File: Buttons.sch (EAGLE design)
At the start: 63 parts, among them T1 SI2301, U1 TCA8418RTWR, U2 Tiny85-20-SMT

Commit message: this could be the one neo!
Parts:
- added R3: 1k, SparkFun-Passives:RESISTOR0805-RES
- R1: value 100 -> 1k
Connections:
- removed net N$49: U1.ROW0
- removed net N$9: U1.ROW1
- new net N$8: R3.2, U1.ROW5, U1.ROW6, U1.ROW7
- net 3V3@2: now also R3.1
- net N$24: now also U1.ROW4; no longer U1.ROW6
- net N$29: now also U1.ROW3; no longer U1.ROW5
- net N$30: now also U1.ROW2; no longer U1.ROW4
- net N$31: now also U1.ROW1; no longer U1.ROW3
- net N$33: now also U1.ROW0; no longer U1.ROW2
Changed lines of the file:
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@@
 <parts>
 <part name="U$2" library="ili9341" deviceset="ILI9341-2.8" device=""/>
-<part name="R1" library="resistor" deviceset="R-EU_" device="R0805" value="100"/>
+<part name="R1" library="resistor" deviceset="R-EU_" device="R0805" value="1k"/>
 <part name="GND3" library="supply1" deviceset="GND" device=""/>
 <part name="PI1" library="RPI-Zero" deviceset="RPI-ZERO" device=""/>
@@
 <part name="U$3" library="5mmSNAP" deviceset="5MMSNAP" device=""/>
 <part name="GND10" library="supply1" deviceset="GND" device=""/>
+<part name="R3" library="SparkFun-Passives" deviceset="RESISTOR" device="0805-RES" value="1k"/>
 </parts>
 <sheets>
@@
 <instance part="GND4" gate="1" x="48.26" y="200.66"/>
 <instance part="GND5" gate="1" x="63.5" y="187.96"/>
-<instance part="GND6" gate="1" x="-53.34" y="78.74" rot="R270"/>
+<instance part="GND6" gate="1" x="-38.1" y="78.74" rot="R270"/>
 <instance part="GND9" gate="1" x="180.34" y="182.88" rot="R90"/>
 <instance part="U1" gate="A" x="-15.24" y="99.06"/>
@@
 <instance part="U$3" gate="G$1" x="93.98" y="210.82" rot="R180"/>
 <instance part="GND10" gate="1" x="182.88" y="233.68" rot="R180"/>
+<instance part="R3" gate="G$1" x="-45.72" y="73.66" rot="R90"/>
 </instances>
 <busses>
@@
 <pinref part="U1" gate="A" pin="GND"/>
 <pinref part="GND6" gate="1" pin="GND"/>
-<wire x1="-50.8" y1="78.74" x2="-33.02" y2="78.74" width="0.1524" layer="91"/>
+<wire x1="-35.56" y1="78.74" x2="-33.02" y2="78.74" width="0.1524" layer="91"/>
 </segment>
 <segment>
@@
 <net name="N$24" class="0">
 <segment>
-<pinref part="U1" gate="A" pin="ROW6"/>
-<wire x1="-33.02" y1="86.36" x2="-35.56" y2="86.36" width="0.1524" layer="91"/>
-<wire x1="-35.56" y1="86.36" x2="-35.56" y2="66.04" width="0.1524" layer="91"/>
-<wire x1="-35.56" y1="66.04" x2="5.08" y2="66.04" width="0.1524" layer="91"/>
+<wire x1="-50.8" y1="91.44" x2="-50.8" y2="66.04" width="0.1524" layer="91"/>
+<wire x1="-50.8" y1="66.04" x2="5.08" y2="66.04" width="0.1524" layer="91"/>
 <wire x1="5.08" y1="66.04" x2="5.08" y2="71.12" width="0.1524" layer="91"/>
 <wire x1="5.08" y1="71.12" x2="33.02" y2="71.12" width="0.1524" layer="91"/>
@@
 <pinref part="A9" gate="G$1" pin="P$2"/>
 <wire x1="147.32" y1="73.66" x2="147.32" y2="71.12" width="0.1524" layer="91"/>
+<pinref part="U1" gate="A" pin="ROW4"/>
+<wire x1="-33.02" y1="91.44" x2="-50.8" y2="91.44" width="0.1524" layer="91"/>
 </segment>
 </net>
 <net name="N$29" class="0">
 <segment>
-<pinref part="U1" gate="A" pin="ROW5"/>
-<wire x1="-38.1" y1="55.88" x2="-38.1" y2="88.9" width="0.1524" layer="91"/>
-<wire x1="-38.1" y1="88.9" x2="-33.02" y2="88.9" width="0.1524" layer="91"/>
+<wire x1="-53.34" y1="55.88" x2="-53.34" y2="93.98" width="0.1524" layer="91"/>
 <wire x1="147.32" y1="55.88" x2="134.62" y2="55.88" width="0.1524" layer="91"/>
 <pinref part="B9" gate="G$1" pin="P$2"/>
@@
 <wire x1="58.42" y1="55.88" x2="45.72" y2="55.88" width="0.1524" layer="91"/>
 <wire x1="45.72" y1="55.88" x2="33.02" y2="55.88" width="0.1524" layer="91"/>
-<wire x1="33.02" y1="55.88" x2="-38.1" y2="55.88" width="0.1524" layer="91"/>
+<wire x1="33.02" y1="55.88" x2="-53.34" y2="55.88" width="0.1524" layer="91"/>
 <wire x1="147.32" y1="58.42" x2="147.32" y2="55.88" width="0.1524" layer="91"/>
 <pinref part="B8" gate="G$1" pin="P$2"/>
@@
 <pinref part="B0" gate="G$1" pin="P$2"/>
 <wire x1="33.02" y1="58.42" x2="33.02" y2="55.88" width="0.1524" layer="91"/>
+<pinref part="U1" gate="A" pin="ROW3"/>
+<wire x1="-33.02" y1="93.98" x2="-53.34" y2="93.98" width="0.1524" layer="91"/>
 </segment>
 </net>
 <net name="N$30" class="0">
 <segment>
-<pinref part="U1" gate="A" pin="ROW4"/>
-<wire x1="-40.64" y1="40.64" x2="-40.64" y2="91.44" width="0.1524" layer="91"/>
-<wire x1="-40.64" y1="91.44" x2="-33.02" y2="91.44" width="0.1524" layer="91"/>
+<wire x1="-55.88" y1="40.64" x2="-55.88" y2="96.52" width="0.1524" layer="91"/>
 <wire x1="147.32" y1="40.64" x2="134.62" y2="40.64" width="0.1524" layer="91"/>
 <pinref part="C0" gate="G$1" pin="P$2"/>
@@
 <wire x1="58.42" y1="40.64" x2="45.72" y2="40.64" width="0.1524" layer="91"/>
 <wire x1="45.72" y1="40.64" x2="33.02" y2="40.64" width="0.1524" layer="91"/>
-<wire x1="33.02" y1="40.64" x2="-40.64" y2="40.64" width="0.1524" layer="91"/>
+<wire x1="33.02" y1="40.64" x2="-55.88" y2="40.64" width="0.1524" layer="91"/>
 <wire x1="33.02" y1="43.18" x2="33.02" y2="40.64" width="0.1524" layer="91"/>
 <pinref part="C1" gate="G$1" pin="P$2"/>
@@
 <pinref part="C9" gate="G$1" pin="P$2"/>
 <wire x1="147.32" y1="43.18" x2="147.32" y2="40.64" width="0.1524" layer="91"/>
+<pinref part="U1" gate="A" pin="ROW2"/>
+<wire x1="-33.02" y1="96.52" x2="-55.88" y2="96.52" width="0.1524" layer="91"/>
 </segment>
 </net>
 <net name="N$31" class="0">
 <segment>
-<pinref part="U1" gate="A" pin="ROW3"/>
-<wire x1="-33.02" y1="93.98" x2="-43.18" y2="93.98" width="0.1524" layer="91"/>
-<wire x1="-43.18" y1="93.98" x2="-43.18" y2="25.4" width="0.1524" layer="91"/>
+<wire x1="-58.42" y1="99.06" x2="-58.42" y2="25.4" width="0.1524" layer="91"/>
 <wire x1="147.32" y1="25.4" x2="134.62" y2="25.4" width="0.1524" layer="91"/>
 <pinref part="D9" gate="G$1" pin="P$2"/>
@@
 <wire x1="58.42" y1="25.4" x2="45.72" y2="25.4" width="0.1524" layer="91"/>
 <wire x1="45.72" y1="25.4" x2="33.02" y2="25.4" width="0.1524" layer="91"/>
-<wire x1="33.02" y1="25.4" x2="-43.18" y2="25.4" width="0.1524" layer="91"/>
+<wire x1="33.02" y1="25.4" x2="-58.42" y2="25.4" width="0.1524" layer="91"/>
 <wire x1="147.32" y1="27.94" x2="147.32" y2="25.4" width="0.1524" layer="91"/>
 <pinref part="D8" gate="G$1" pin="P$2"/>
@@
 <pinref part="D0" gate="G$1" pin="P$2"/>
 <wire x1="33.02" y1="27.94" x2="33.02" y2="25.4" width="0.1524" layer="91"/>
+<pinref part="U1" gate="A" pin="ROW1"/>
+<wire x1="-33.02" y1="99.06" x2="-58.42" y2="99.06" width="0.1524" layer="91"/>
 </segment>
 </net>
 <net name="N$33" class="0">
 <segment>
-<pinref part="U1" gate="A" pin="ROW2"/>
-<wire x1="-45.72" y1="10.16" x2="-45.72" y2="96.52" width="0.1524" layer="91"/>
-<wire x1="-45.72" y1="96.52" x2="-33.02" y2="96.52" width="0.1524" layer="91"/>
+<wire x1="-60.96" y1="10.16" x2="-60.96" y2="101.6" width="0.1524" layer="91"/>
 <wire x1="147.32" y1="10.16" x2="134.62" y2="10.16" width="0.1524" layer="91"/>
 <pinref part="E0" gate="G$1" pin="P$2"/>
@@
 <wire x1="58.42" y1="10.16" x2="45.72" y2="10.16" width="0.1524" layer="91"/>
 <wire x1="45.72" y1="10.16" x2="33.02" y2="10.16" width="0.1524" layer="91"/>
-<wire x1="33.02" y1="10.16" x2="-45.72" y2="10.16" width="0.1524" layer="91"/>
+<wire x1="33.02" y1="10.16" x2="-60.96" y2="10.16" width="0.1524" layer="91"/>
 <wire x1="33.02" y1="12.7" x2="33.02" y2="10.16" width="0.1524" layer="91"/>
 <pinref part="E1" gate="G$1" pin="P$2"/>
@@
 <pinref part="E9" gate="G$1" pin="P$2"/>
 <wire x1="147.32" y1="12.7" x2="147.32" y2="10.16" width="0.1524" layer="91"/>
+<pinref part="U1" gate="A" pin="ROW0"/>
+<wire x1="-33.02" y1="101.6" x2="-60.96" y2="101.6" width="0.1524" layer="91"/>
 </segment>
 </net>
@@
 </segment>
 </net>
-<net name="N$9" class="0">
-<segment>
-<pinref part="U1" gate="A" pin="ROW1"/>
-<wire x1="-48.26" y1="99.06" x2="-33.02" y2="99.06" width="0.1524" layer="91"/>
-</segment>
-</net>
-<net name="N$49" class="0">
-<segment>
-<pinref part="U1" gate="A" pin="ROW0"/>
-<wire x1="-50.8" y1="101.6" x2="-33.02" y2="101.6" width="0.1524" layer="91"/>
-</segment>
-</net>
 <net name="N$10" class="0">
 <segment>
@@
 <pinref part="U1" gate="A" pin="VCC"/>
 <pinref part="PI1" gate="G$1" pin="3V3@2"/>
-<wire x1="-33.02" y1="177.8" x2="-33.02" y2="114.3" width="0.1524" layer="91"/>
+<wire x1="-33.02" y1="177.8" x2="-33.02" y2="124.46" width="0.1524" layer="91"/>
+<wire x1="-33.02" y1="124.46" x2="-33.02" y2="114.3" width="0.1524" layer="91"/>
 <wire x1="106.68" y1="177.8" x2="-33.02" y2="177.8" width="0.1524" layer="91"/>
-</segment>
-</net>
+<wire x1="-45.72" y1="68.58" x2="-15.24" y2="68.58" width="0.1524" layer="91"/>
+<wire x1="-15.24" y1="68.58" x2="-15.24" y2="124.46" width="0.1524" layer="91"/>
+<wire x1="-15.24" y1="124.46" x2="-33.02" y2="124.46" width="0.1524" layer="91"/>
+<pinref part="R3" gate="G$1" pin="1"/>
+</segment>
+</net>
+<net name="N$8" class="0">
+<segment>
+<pinref part="U1" gate="A" pin="ROW5"/>
+<wire x1="-33.02" y1="88.9" x2="-45.72" y2="88.9" width="0.1524" layer="91"/>
+<wire x1="-45.72" y1="88.9" x2="-45.72" y2="86.36" width="0.1524" layer="91"/>
+<pinref part="U1" gate="A" pin="ROW7"/>
+<pinref part="U1" gate="A" pin="ROW6"/>
+<wire x1="-33.02" y1="86.36" x2="-45.72" y2="86.36" width="0.1524" layer="91"/>
+<wire x1="-45.72" y1="78.74" x2="-45.72" y2="83.82" width="0.1524" layer="91"/>
+<wire x1="-45.72" y1="83.82" x2="-45.72" y2="86.36" width="0.1524" layer="91"/>
+<wire x1="-33.02" y1="83.82" x2="-45.72" y2="83.82" width="0.1524" layer="91"/>
+<pinref part="R3" gate="G$1" pin="2"/>
+</segment>
+</net>

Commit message: nailed it!
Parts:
- added INT, RST: TPB2,54, testpad:TPB2,54
- renumbered CN1 to BAT
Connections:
- new net N$15: INT.TP, U1.~INT
- new net N$16: RST.TP, U1.~RESET
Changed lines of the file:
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@@
 <part name="U1" library="Texas Instruments_By_element14_Batch_1" deviceset="TCA8418RTWR" device=""/>
 <part name="U$1" library="03962A" deviceset="03962A" device=""/>
-<part name="CN1" library="adafruit" deviceset="JST_2PIN" device="-SMT-RA"/>
+<part name="BAT" library="adafruit" deviceset="JST_2PIN" device="-SMT-RA"/>
 <part name="A1" library="5mmSNAP" deviceset="5MMSNAP" device=""/>
 <part name="A2" library="5mmSNAP" deviceset="5MMSNAP" device=""/>
@@
 <part name="GND10" library="supply1" deviceset="GND" device=""/>
 <part name="R3" library="SparkFun-Passives" deviceset="RESISTOR" device="0805-RES" value="1k"/>
+<part name="INT" library="testpad" deviceset="TP" device="B2,54"/>
+<part name="RST" library="testpad" deviceset="TP" device="B2,54"/>
 </parts>
 <sheets>
@@
 <instance part="U1" gate="A" x="-15.24" y="99.06"/>
 <instance part="U$1" gate="G$1" x="195.58" y="220.98" rot="R180"/>
-<instance part="CN1" gate="G$1" x="175.26" y="218.44"/>
+<instance part="BAT" gate="G$1" x="175.26" y="218.44"/>
 <instance part="A1" gate="G$1" x="43.18" y="78.74"/>
 <instance part="A2" gate="G$1" x="55.88" y="78.74"/>
@@
 <instance part="GND10" gate="1" x="182.88" y="233.68" rot="R180"/>
 <instance part="R3" gate="G$1" x="-45.72" y="73.66" rot="R90"/>
+<instance part="INT" gate="G$1" x="2.54" y="132.08"/>
+<instance part="RST" gate="G$1" x="-35.56" y="132.08"/>
 </instances>
 <busses>
@@
 <segment>
 <pinref part="U$1" gate="G$1" pin="B+"/>
-<pinref part="CN1" gate="G$1" pin="2"/>
+<pinref part="BAT" gate="G$1" pin="2"/>
 <wire x1="182.88" y1="218.44" x2="177.8" y2="218.44" width="0.1524" layer="91"/>
 <wire x1="172.72" y1="218.44" x2="172.72" y2="213.36" width="0.1524" layer="91"/>
@@
 <net name="N$37" class="0">
 <segment>
-<pinref part="CN1" gate="G$1" pin="1"/>
+<pinref part="BAT" gate="G$1" pin="1"/>
 <wire x1="172.72" y1="220.98" x2="172.72" y2="226.06" width="0.1524" layer="91"/>
 <pinref part="U$1" gate="G$1" pin="B-"/>
@@
 </segment>
 </net>
+<net name="N$15" class="0">
+<segment>
+<pinref part="INT" gate="G$1" pin="TP"/>
+<pinref part="U1" gate="A" pin="~INT"/>
+<wire x1="2.54" y1="129.54" x2="2.54" y2="114.3" width="0.1524" layer="91"/>
+</segment>
+</net>
+<net name="N$16" class="0">
+<segment>
+<pinref part="RST" gate="G$1" pin="TP"/>
+<wire x1="-35.56" y1="129.54" x2="-35.56" y2="109.22" width="0.1524" layer="91"/>
+<pinref part="U1" gate="A" pin="~RESET"/>
+<wire x1="-33.02" y1="109.22" x2="-35.56" y2="109.22" width="0.1524" layer="91"/>
+</segment>
+</net>

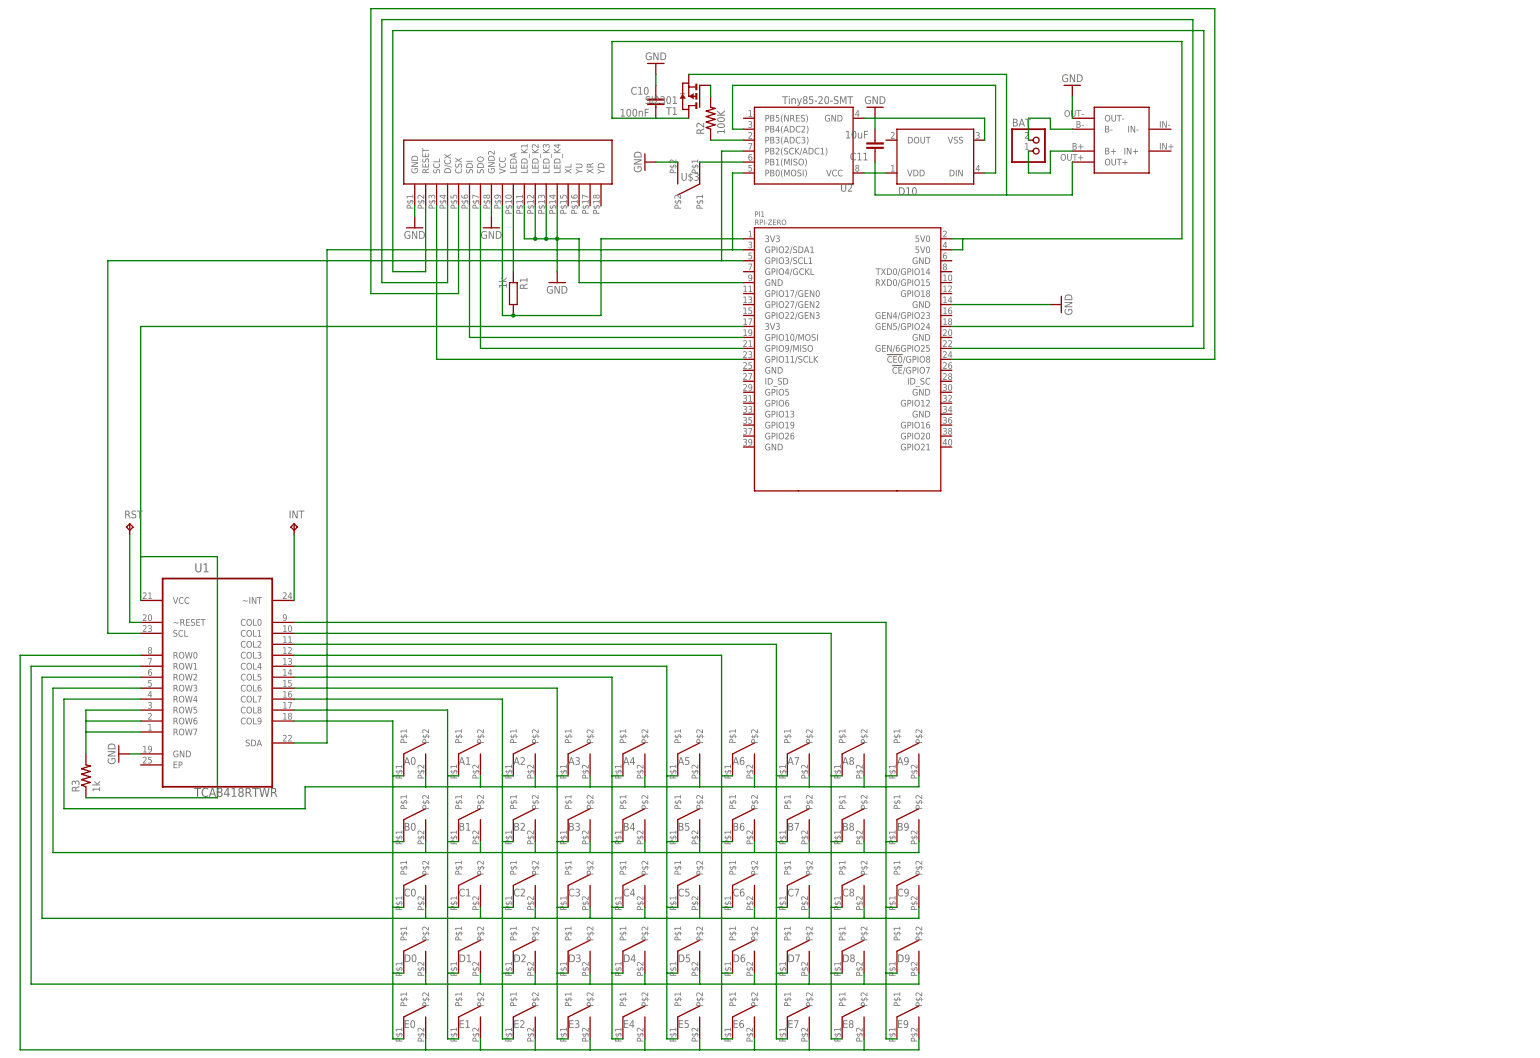
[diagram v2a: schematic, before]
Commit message: changed the tiny85 to a tiny88, the power button is now a side press jobby, and moved to the back along with the neopixel.
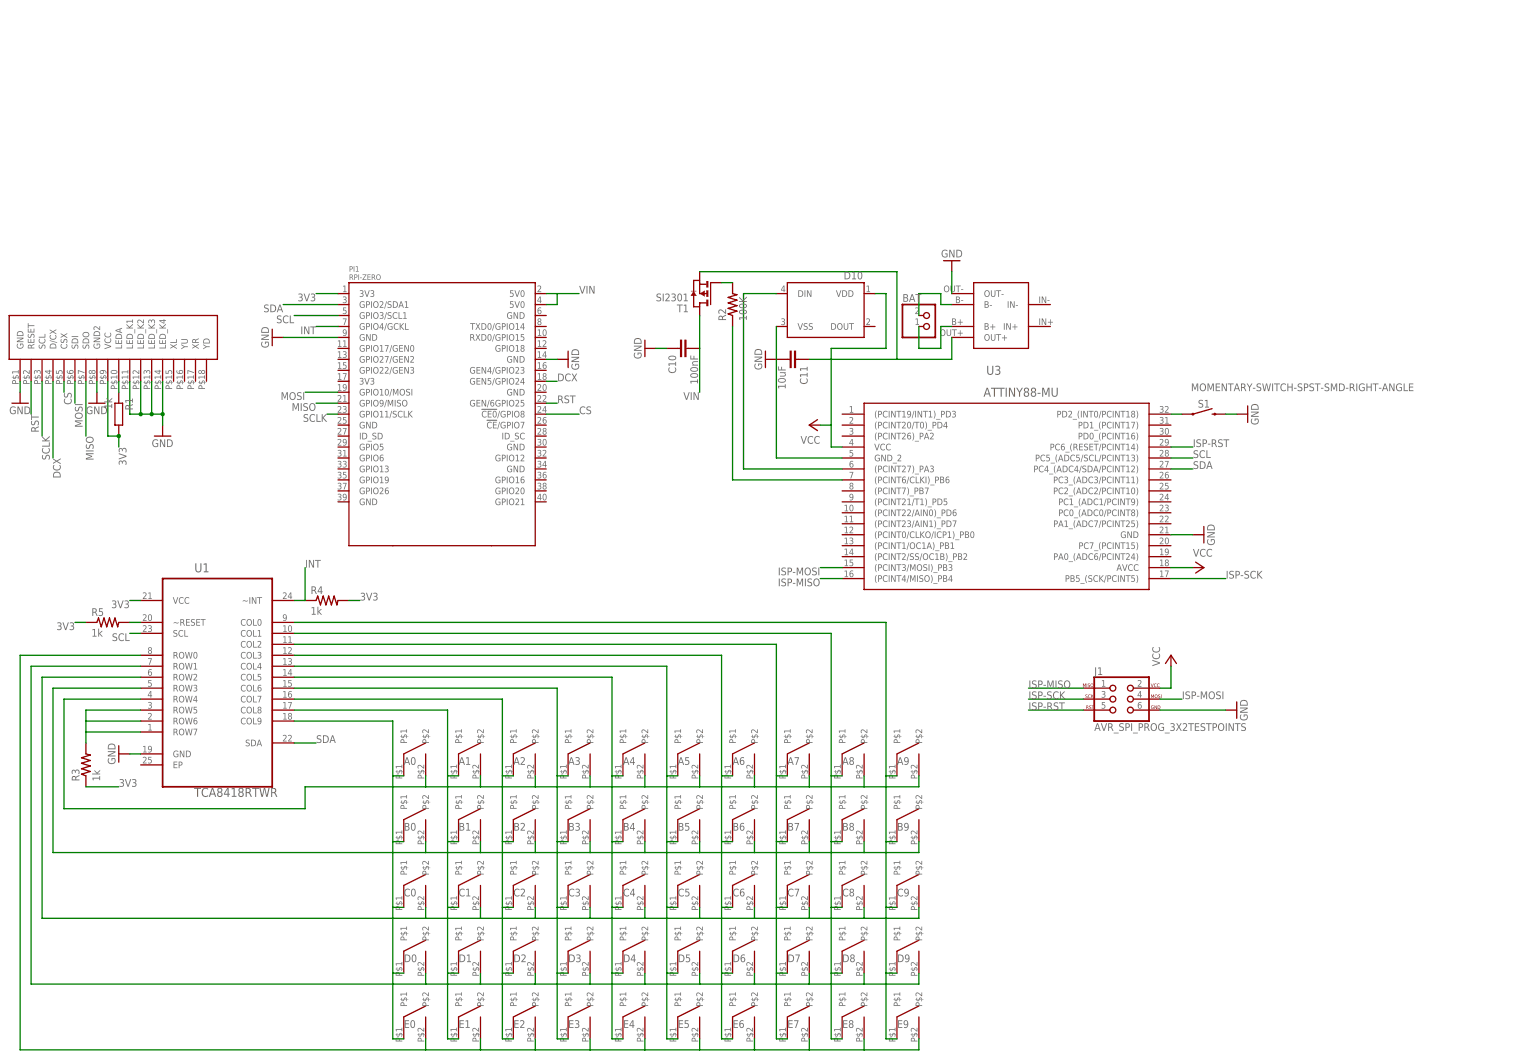
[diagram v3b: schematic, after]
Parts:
- removed INT, RST: TPB2,54, testpad:TPB2,54
- removed U$3: 5MMSNAP, 5mmSNAP:5MMSNAP
- removed U2: Tiny85-20-SMT, SparkFun-DigitalIC:ATTINY45TINY85-20-SMT
- added J1: AVR_SPI_PROG_3X2TESTPOINTS, SparkFun-Connectors:AVR_SPI_PROG_3X2TESTPOINTS
- added R4, R5: 1k, SparkFun-Passives:RESISTOR0805-RES
- added S1: MOMENTARY-SWITCH-SPST-SMD-RIGHT-ANGLE, SparkFun-Switches:MOMENTARY-SWITCH-SPST-SMD-RIGHT-ANGLE
- added U3: ATTINY88-MU, attiny88:ATTINY88-MU
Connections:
- net 5V0@2 renamed VIN
- net N$1 renamed RST
- net N$2 renamed SCLK
- net N$3 renamed MOSI
- net N$4 renamed MISO
- net N$6 renamed DCX
- net N$7 renamed CS
- removed net 3V3@1: PI1.3V3@1, R1.2, U$2.VCC
- removed net 3V3@2: PI1.3V3@2, R3.1, U1.VCC
- removed net GND@1: PI1.GND@1, U$2.LED_K1, U$2.LED_K2, U$2.LED_K3, U$2.LED_K4
- removed net N$11: C11.1, D10.VDD, T1.S, U$1.OUT+, U2.VCC
- removed net N$12: U$3.P$1, U2.PB1(MISO)
- removed net N$15: INT.TP, U1.~INT
- removed net N$18: D10.DIN, U2.PB4(ADC2)
- removed net N$28: PI1.GPIO2/SDA1, U1.SDA, U2.PB0(MOSI)
- removed net N$34: PI1.GPIO3/SCL1, U1.SCL, U2.PB2(SCK/ADC1)
- new net 3V3: PI1.3V3@1, R1.2, R3.1, R4.2, R5.1, U$2.VCC, U1.VCC
- new net INT: PI1.GPIO4/GCKL, R4.1, U1.~INT
- new net ISP-MISO: J1.1, U3.(PCINT4/MISO)_PB4
- new net ISP-MOSI: J1.4, U3.(PCINT3/MOSI)_PB3
- new net ISP-RST: J1.5, U3.PC6_(RESET/PCINT14)
- new net ISP-SCK: J1.3, U3.PB5_(SCK/PCINT5)
- new net N$1: S1.1, U3.PD2_(INT0/PCINT18)
- new net N$2: D10.DIN, U3.(PCINT27)_PA3
- new net SCL: PI1.GPIO3/SCL1, U1.SCL, U3.PC5_(ADC5/SCL/PCINT13)
- new net SDA: PI1.GPIO2/SDA1, U1.SDA, U3.PC4_(ADC4/SDA/PCINT12)
- new net VCC: C11.1, D10.VDD, J1.2, T1.S, U$1.OUT+, U3.AVCC, U3.VCC
- net GND: now also J1.6, PI1.GND@1, S1.2, U$2.LED_K1, U$2.LED_K2, U$2.LED_K3, U$2.LED_K4, U3.GND, U3.GND_2; no longer U$3.P$2, U2.GND
- net N$16: now also R5.2; no longer RST.TP
- net N$19: now also U3.(PCINT6/CLKI)_PB6; no longer U2.PB3(ADC3)
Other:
- moved on the sheet: BAT, C10, C11, D10, PI1, R1, R2, R3, T1
